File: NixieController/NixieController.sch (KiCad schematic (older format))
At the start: 77 parts, among them J1 Conn_01x07, J10 Conn_01x06, J11 Conn_01x05, J12 Barrel_Jack, J13 Conn_01x07, J14 Conn_01x07, J15 Conn_01x07, J2 Conn_01x01, J3 Conn_01x01, J4 Conn_01x01, J5 Conn_01x01, J6 Conn_01x04, J7 Conn_01x04, J8 Conn_01x04, J9 Conn_01x04, Q1 2N2222A, Q2 2N2222A, Q3 2N2222A, SW1 SW_Push, SW2 SW_Push, SW3 SW_Push, U2 L7805

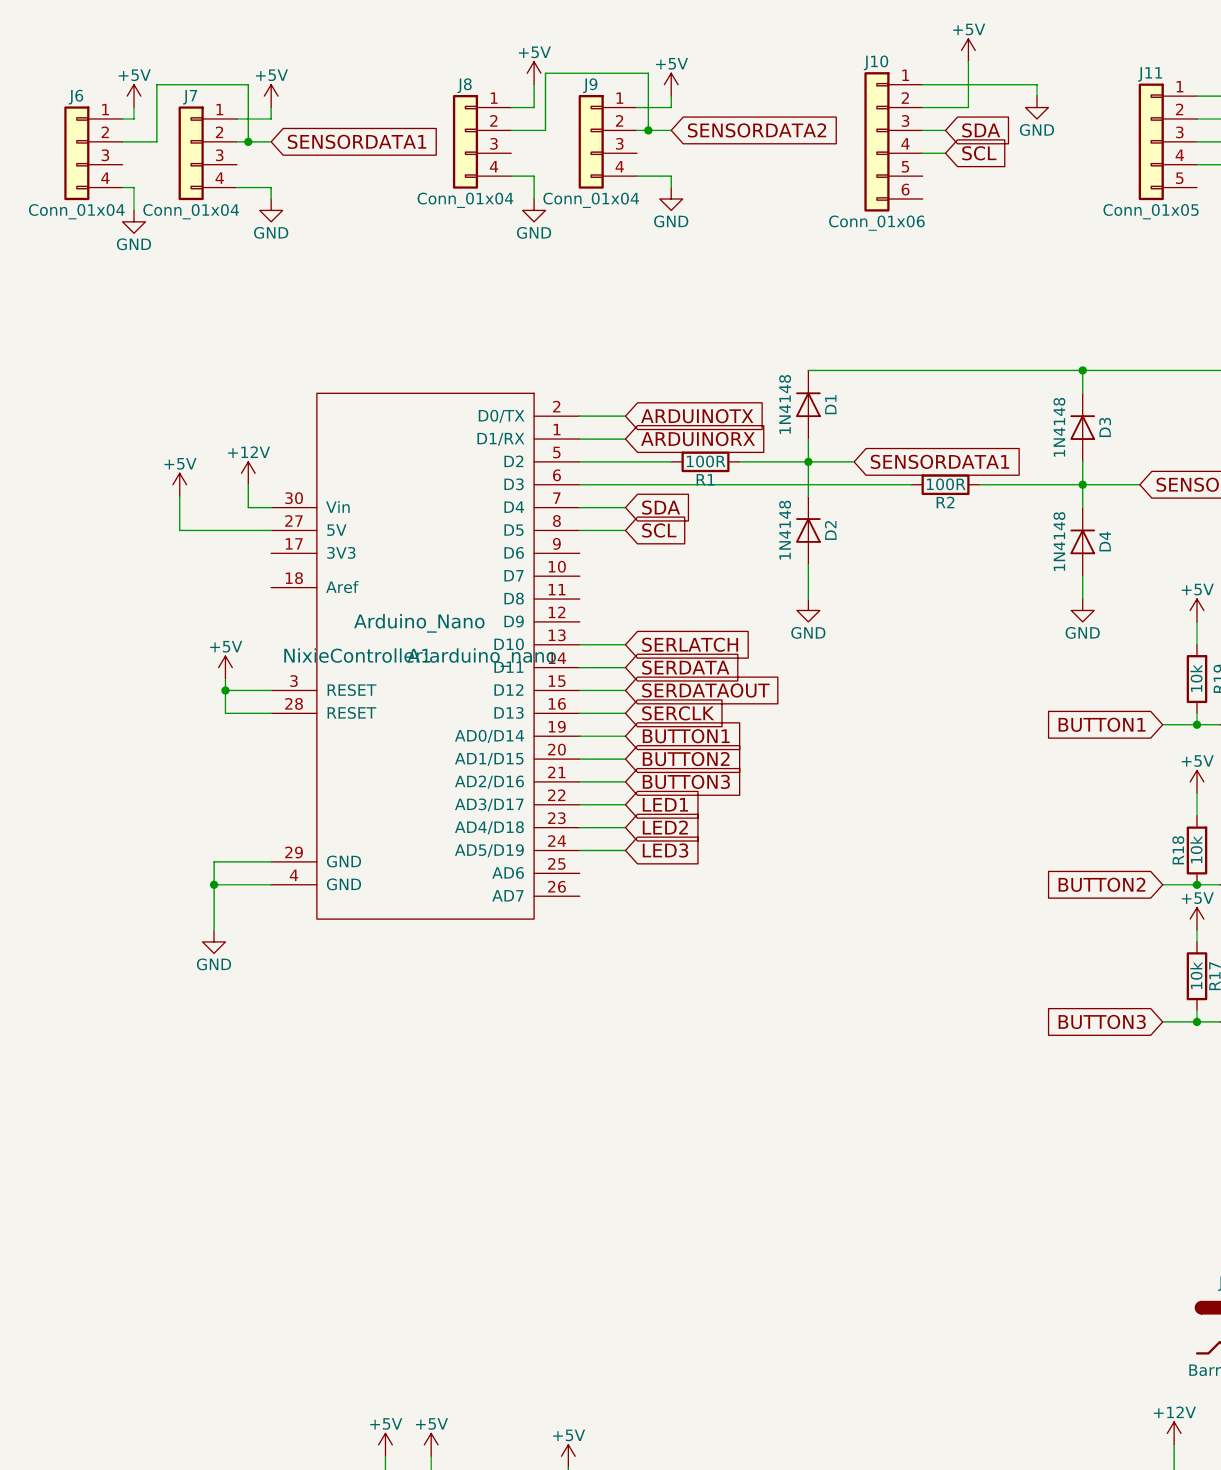
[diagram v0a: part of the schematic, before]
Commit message: First usable version of Nixie Tube Clock
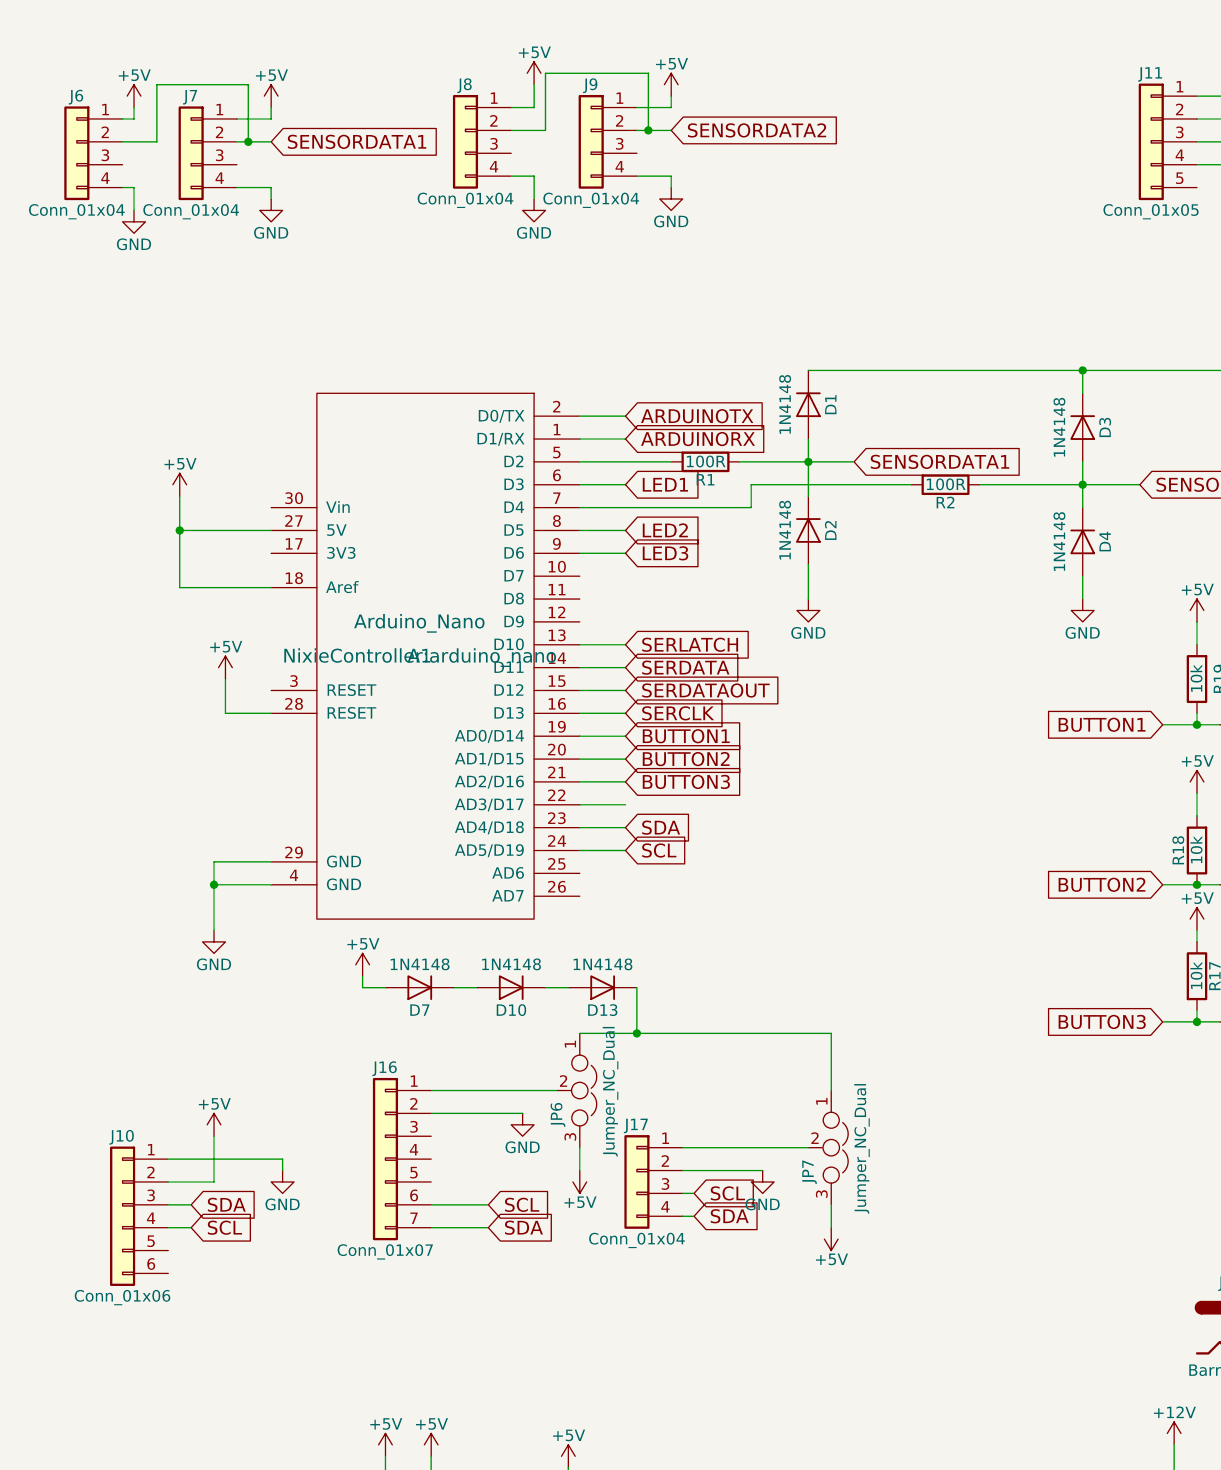
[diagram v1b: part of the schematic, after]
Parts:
- added D10, D13, D7: 1N4148, Diodes_THT:D_DO-35_SOD27_P7.62mm_Horizontal, symbol D
- added J16: Conn_01x07, Pin_Headers:Pin_Header_Straight_1x07_Pitch2.54mm, symbol Conn_01x07
- added J17: Conn_01x04, Pin_Headers:Pin_Header_Straight_1x04_Pitch2.54mm, symbol Conn_01x04
- added JP6, JP7: Jumper_NC_Dual, Pin_Headers:Pin_Header_Straight_1x03_Pitch2.54mm, symbol Jumper_NC_Dual
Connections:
- net +12V: no longer A1.30 (Vin)
- net +5V: now also A1.18 (Aref), D7.2 (A), JP6.3, JP7.3; no longer A1.3 (RESET)
- net GND: now also J16.2 (Pin_2), J17.2 (Pin_2)
- net LED1: now also A1.6 (D3); no longer A1.22 (AD3/D17)
- net LED2: now also A1.8 (D5); no longer A1.23 (AD4/D18)
- net LED3: now also A1.9 (D6); no longer A1.24 (AD5/D19)
- net SCL: now also A1.24 (AD5/D19), J16.6 (Pin_6), J17.3 (Pin_3); no longer A1.8 (D5)
- net SDA: now also A1.23 (AD4/D18), J16.7 (Pin_7), J17.4 (Pin_4); no longer A1.7 (D4)
- net at R2.2: now also A1.7 (D4); no longer A1.6 (D3)
- new net: J17.1 (Pin_1), JP7.2
- new net: J16.1 (Pin_1), JP6.2
- new net: D13.1 (K), JP6.1, JP7.1
- new net: D10.1 (K), D13.2 (A)
- new net: D10.2 (A), D7.1 (K)
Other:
- moved on the sheet: J10

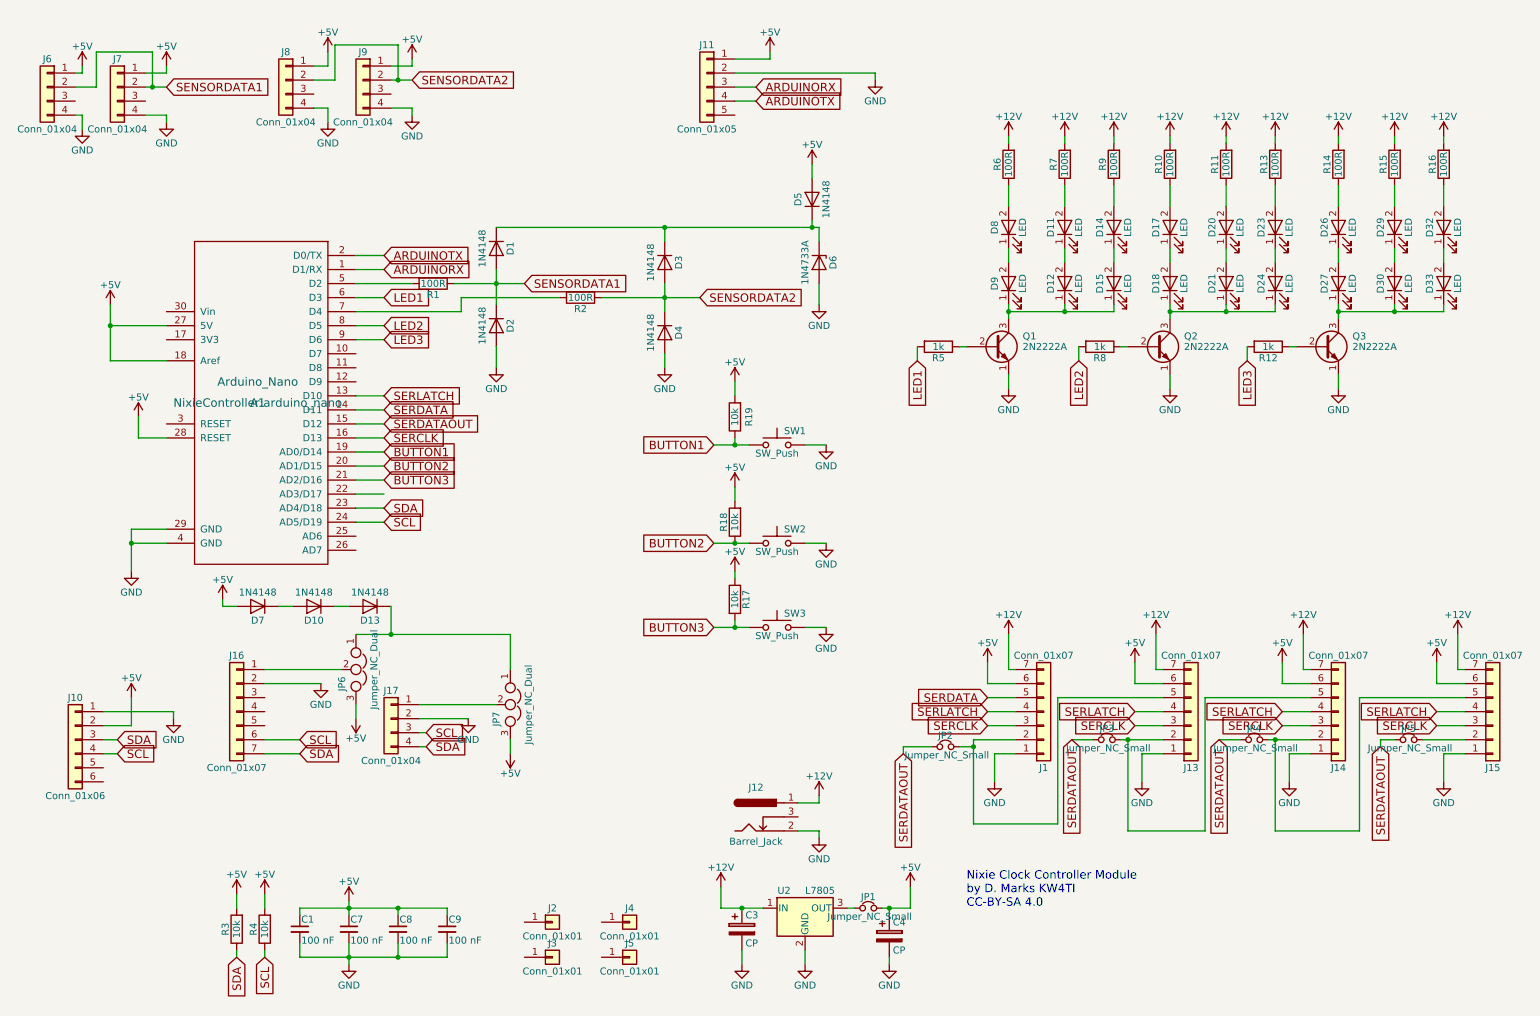
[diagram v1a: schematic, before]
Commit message: Added speaker output
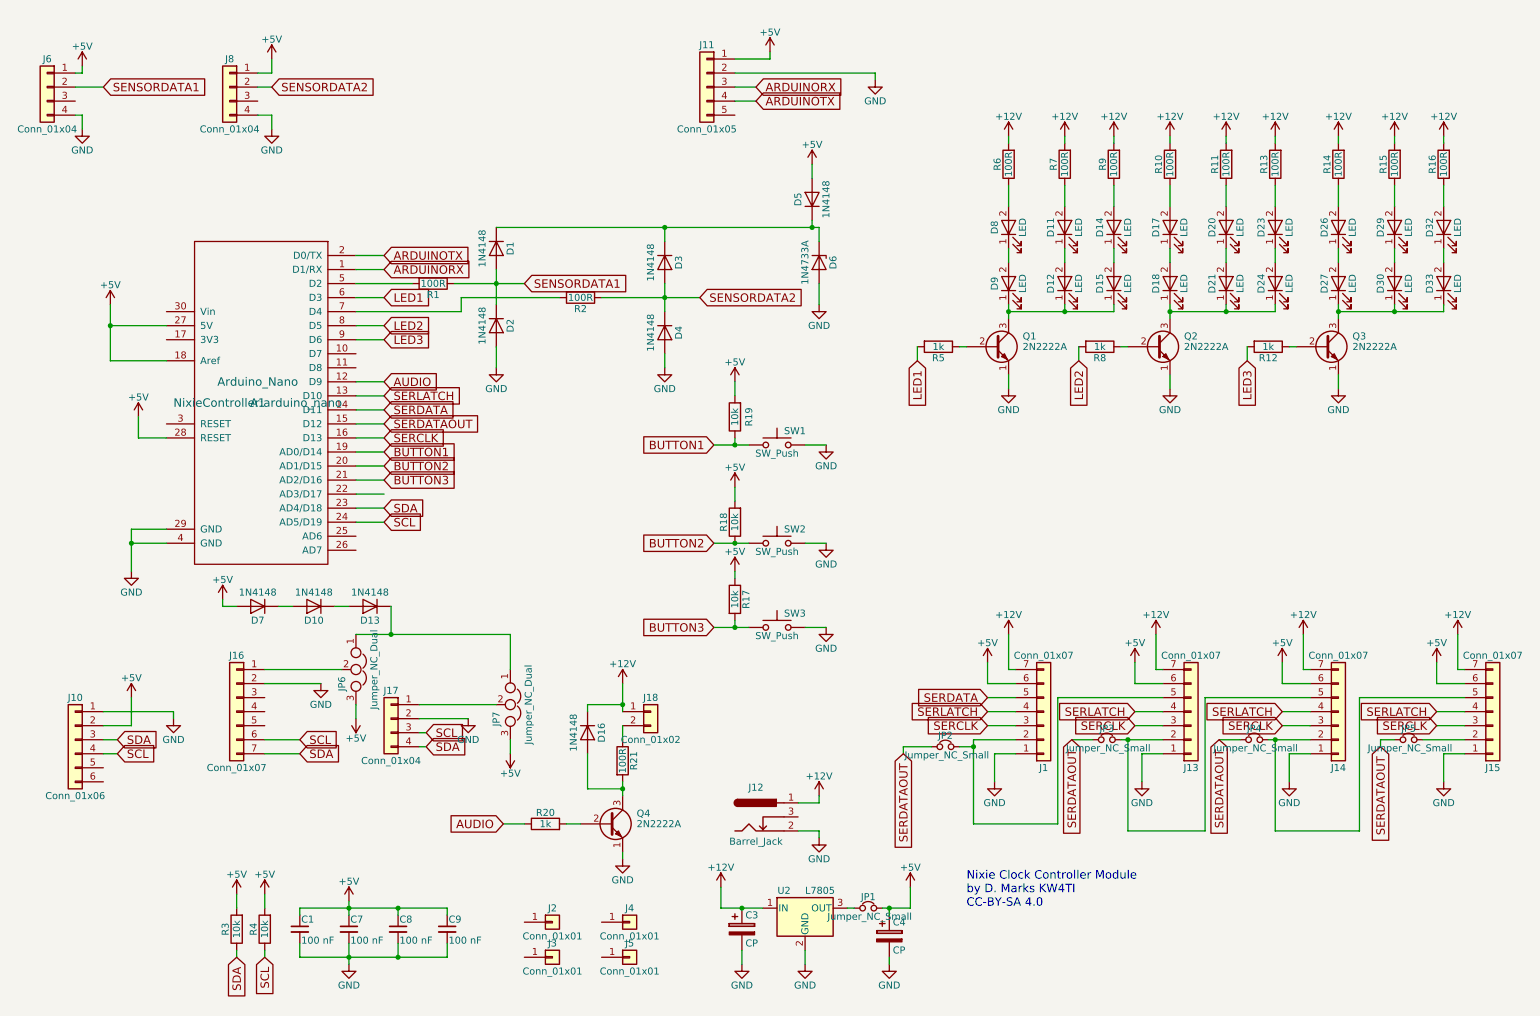
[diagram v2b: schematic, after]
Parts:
- removed J7, J9: Conn_01x04, Pin_Headers:Pin_Header_Straight_1x04_Pitch2.00mm, symbol Conn_01x04
- added D16: 1N4148, Diodes_THT:D_DO-35_SOD27_P7.62mm_Horizontal, symbol D
- added J18: Conn_01x02, Connectors_Molex:Molex_KK-6410-02_02x2.54mm_Straight, symbol Conn_01x02
- added Q4: 2N2222A, TO_SOT_Packages_THT:TO-92_Molded_Narrow, symbol 2N3904
- added R20: 1k, Resistors_THT:R_Axial_DIN0207_L6.3mm_D2.5mm_P7.62mm_Horizontal, symbol R
- added R21: 100R, Resistors_THT:R_Axial_DIN0207_L6.3mm_D2.5mm_P7.62mm_Horizontal, symbol R
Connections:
- net +12V: now also D16.1 (K), J18.1 (Pin_1)
- net GND: now also Q4.1 (E)
- net AUDIO: now reaches A1.12 (D9)
- net AUDIO: now also R20.1
- new net: Q4.2 (B), R20.2
- new net: D16.2 (A), Q4.3 (C), R21.2
- new net: J18.2 (Pin_2), R21.1
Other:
- moved on the sheet: J8

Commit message: Changed connector between boards to 10 pin IDC, added Bill of Materials
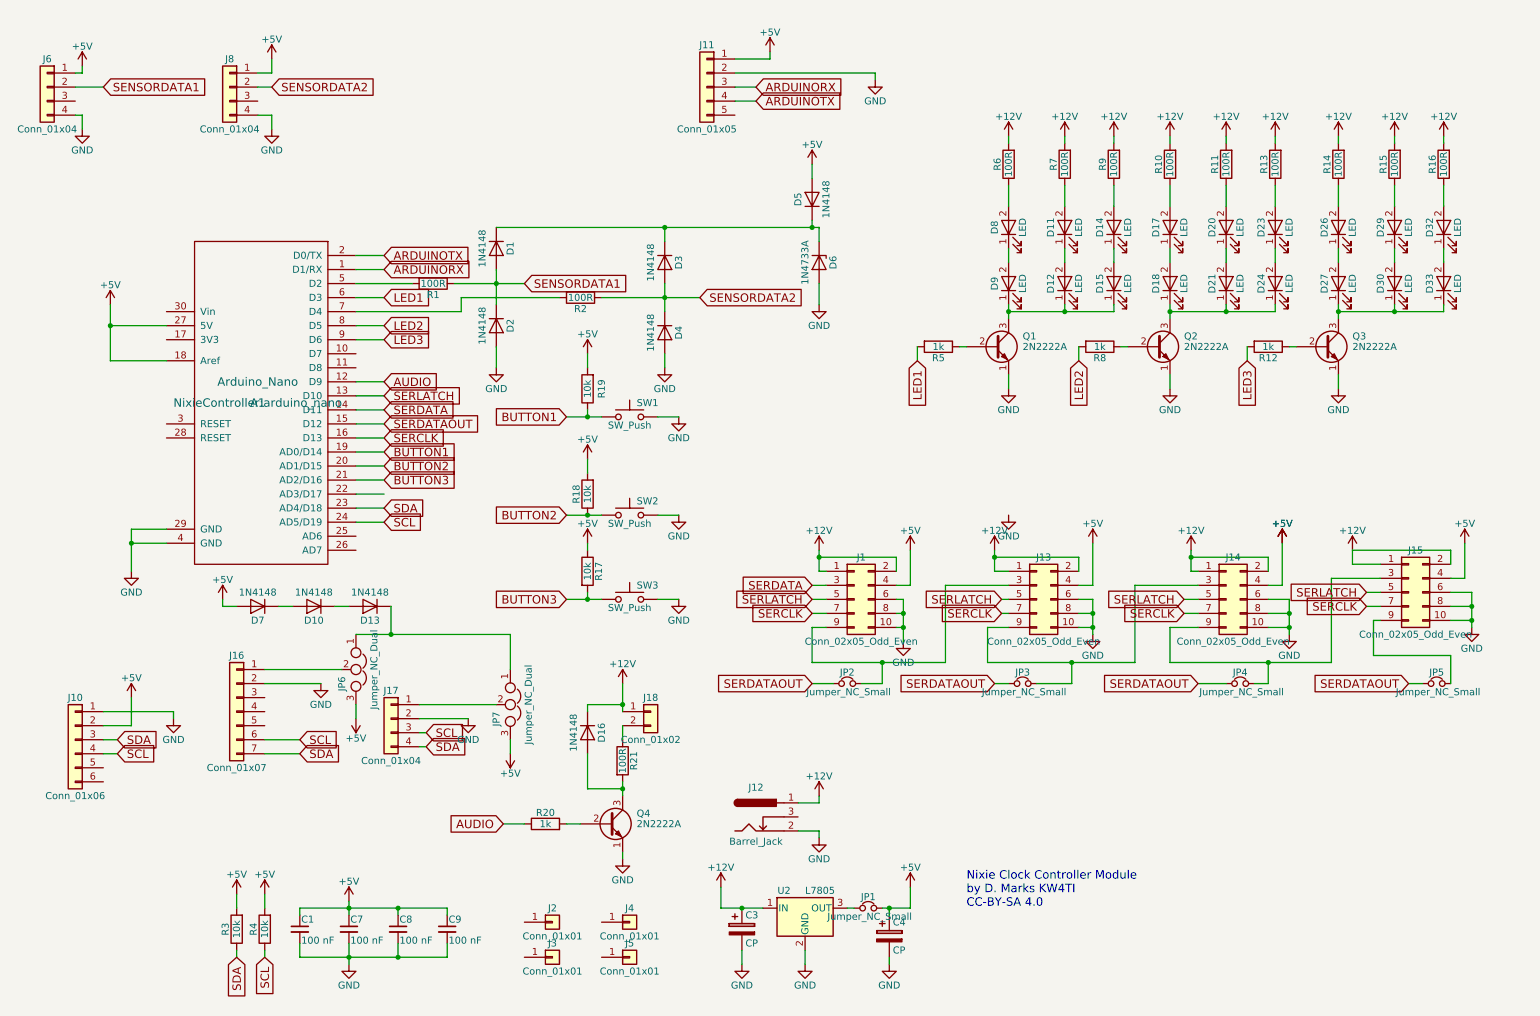
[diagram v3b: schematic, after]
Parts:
- removed J1, J13, J14, J15: Conn_01x07, Connectors_Molex:Molex_KK-6410-07_07x2.54mm_Straight, symbol Conn_01x07
- added J1, J13, J14, J15: Conn_02x05_Odd_Even, Pin_Headers:Pin_Header_Straight_2x05_Pitch2.54mm, symbol Conn_02x05_Odd_Even
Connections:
- net +12V: now also J1.1 (Pin_1), J1.2 (Pin_2), J13.1 (Pin_1), J13.2 (Pin_2), J14.1 (Pin_1), J14.2 (Pin_2), J15.1 (Pin_1), J15.2 (Pin_2)
- net +5V: now also J1.4 (Pin_4), J13.4 (Pin_4), J14.4 (Pin_4), J15.4 (Pin_4); no longer A1.28 (RESET)
- net GND: now also J1.10 (Pin_10), J1.6 (Pin_6), J1.8 (Pin_8), J13.10 (Pin_10), J13.6 (Pin_6), J13.8 (Pin_8), J14.10 (Pin_10), J14.6 (Pin_6), J14.8 (Pin_8), J15.10 (Pin_10), J15.6 (Pin_6), J15.8 (Pin_8)
- net SERCLK: now also J1.7 (Pin_7), J13.7 (Pin_7), J14.7 (Pin_7), J15.7 (Pin_7)
- net SERDATA: now also J1.3 (Pin_3)
- net SERLATCH: now also J1.5 (Pin_5), J13.5 (Pin_5), J14.5 (Pin_5), J15.5 (Pin_5)
- net at JP2.2: now also J1.9 (Pin_9), J13.3 (Pin_3)
- net at JP3.2: now also J13.9 (Pin_9), J14.3 (Pin_3)
- net at JP4.2: now also J14.9 (Pin_9), J15.3 (Pin_3)
- net at JP5.2: now also J15.9 (Pin_9)
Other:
- moved on the sheet: JP2, JP3, JP4, JP5, R17, R18, R19, SW1, SW2, SW3
